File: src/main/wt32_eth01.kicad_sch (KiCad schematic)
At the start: 14 parts, among them J101 Conn_01x10, J105 Conn_01x06, U101 CD74HCT125M96, U202 WT32-ETH01-M3

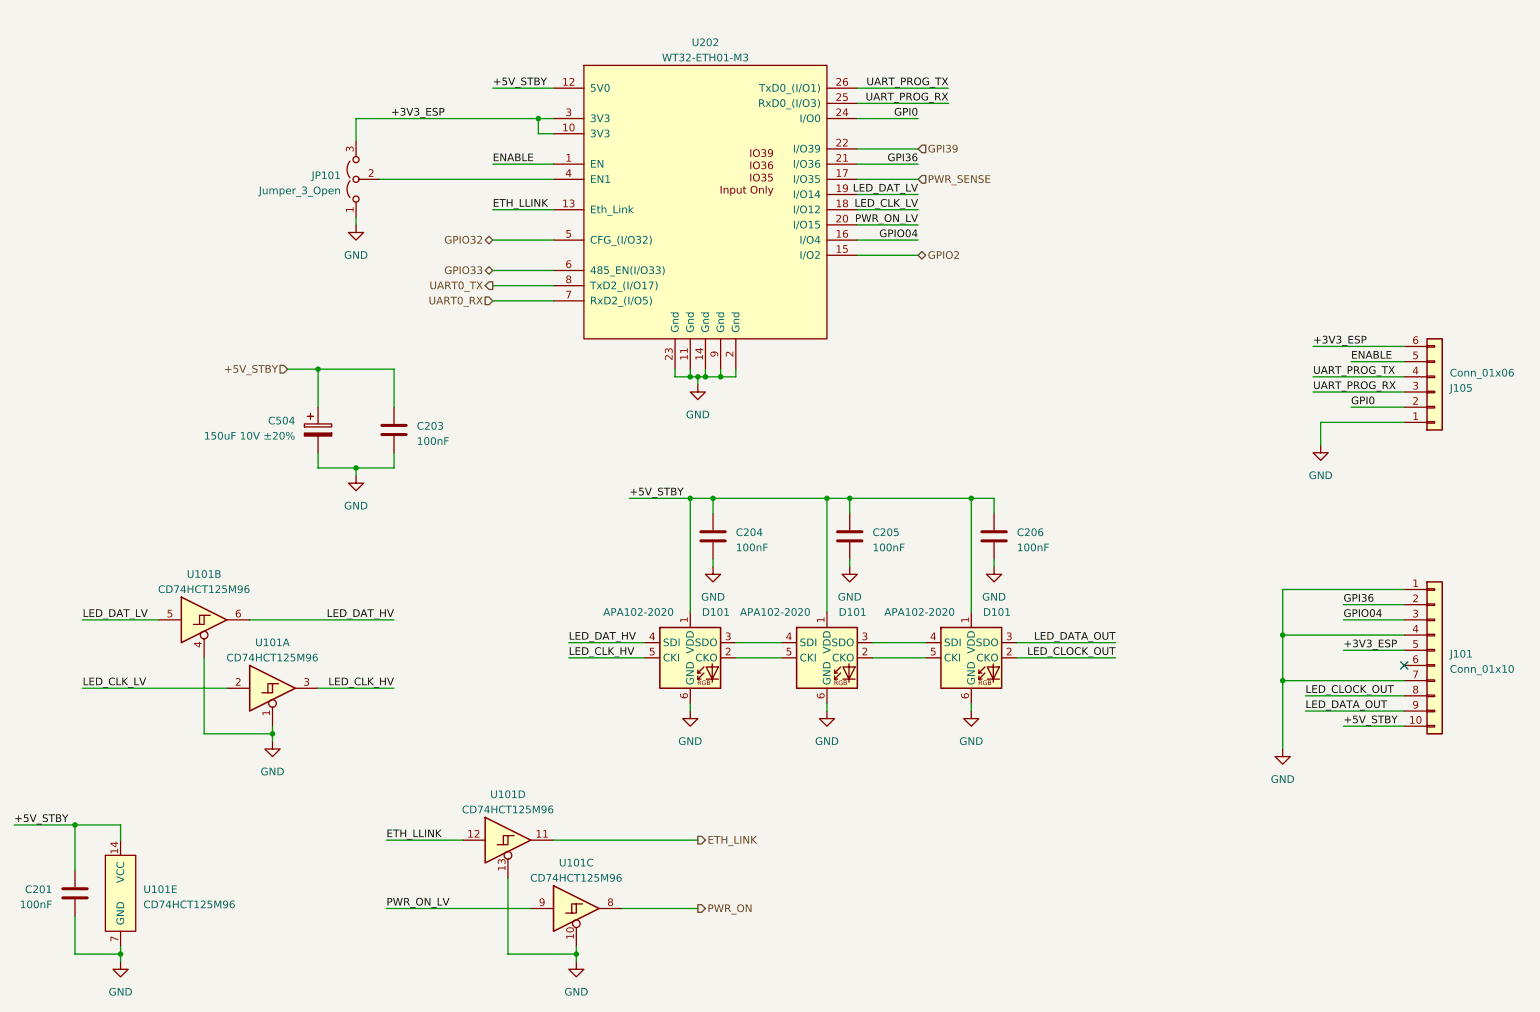
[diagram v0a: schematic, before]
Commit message: rev1.1.0
- J201 programming header
  - Add reset button
  - Add enable button
  - Make pinout compatible with USB-UART boards
    - Move GPI0 and ENABLE to testpoints
- Add power rail LED status indicators
  - 3V3_RUN
  - 3V3_ESP32
  - 5V_RUN
  - 5V_STBY
  - VBUS_[1-3]
- Remove JP201
- Add GPIO39 external pullup to 3V3
- Add pulldown to PWR_BUTTON (GPIO15)
- Add github link
- Add sillkscreen alignment fixes
- Add silkscreen default jumper marking
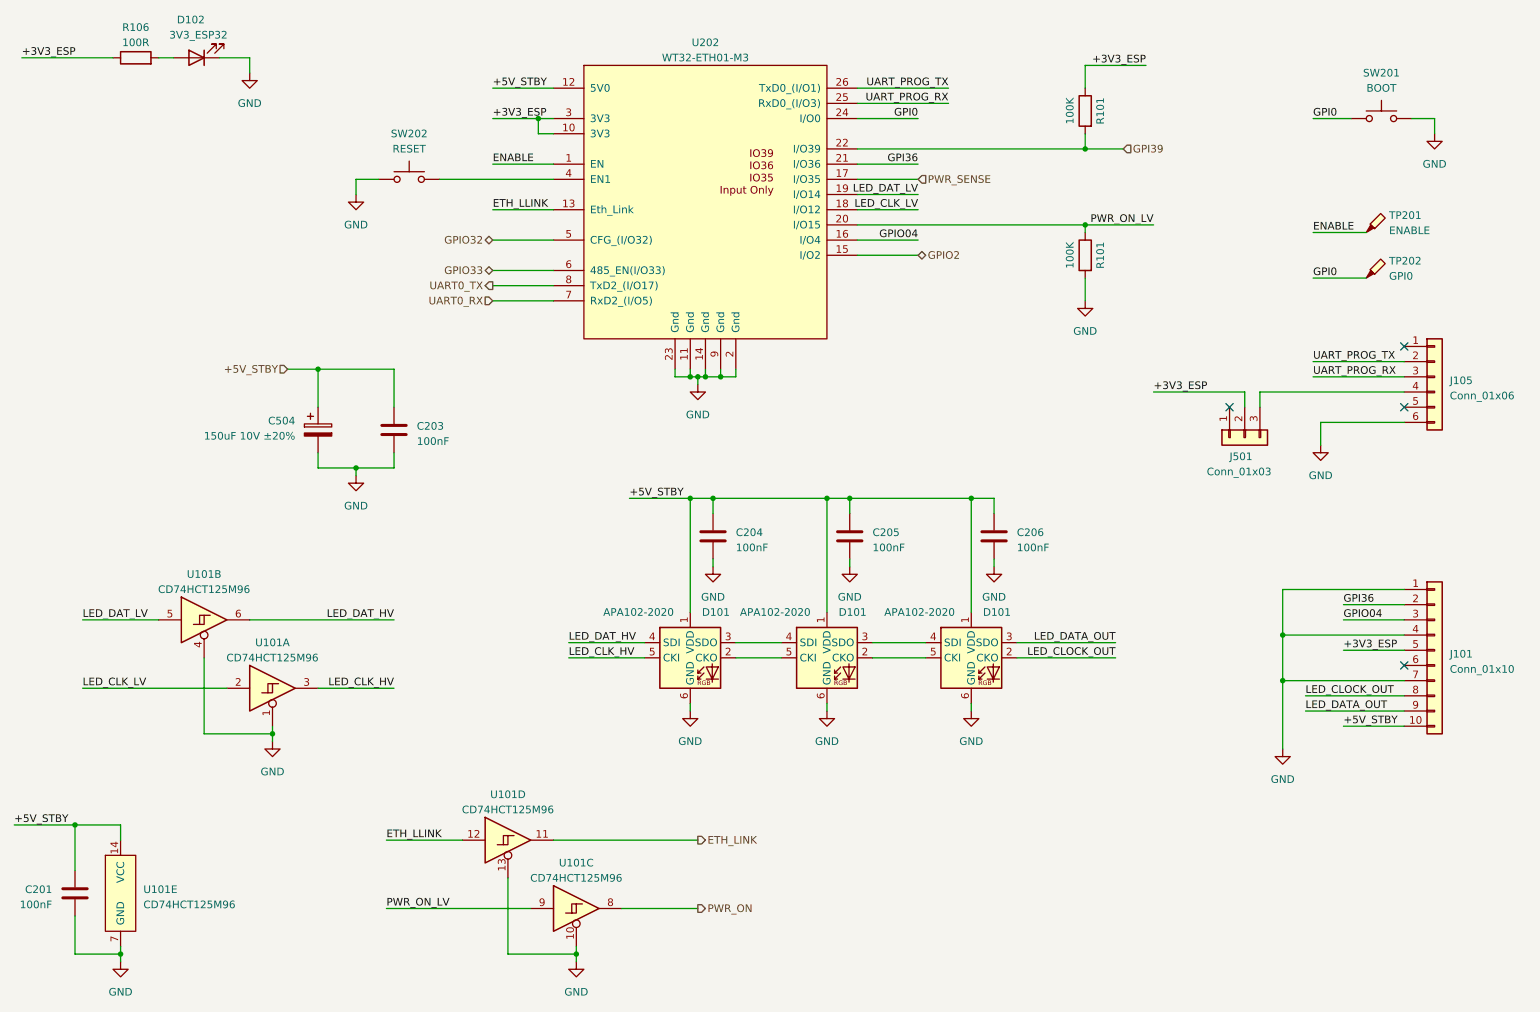
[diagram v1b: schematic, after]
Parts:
- removed JP101: Jumper_3_Open, Jumper:SolderJumper-3_P1.3mm_Open_RoundedPad1.0x1.5mm_NumberLabels, symbol Jumper:Jumper_3_Open
- added D102: 3V3_ESP32, LED_SMD:LED_0603_1608Metric, symbol Device:LED
- added J501: Conn_01x03, odroid_h3_uitx_adapter:PinHeader_1x03_P2.54mm_Vertical, symbol odroid_h3_uitx_adapter:Conn_01x03
- added R101 (x2): 100K, Resistor_SMD:R_0402_1005Metric, symbol Device:R
- added R106: 100R, Resistor_SMD:R_0402_1005Metric, symbol Device:R
- added SW201: BOOT, Button_Switch_THT:SW_PUSH_6mm_H5mm, symbol Switch:SW_Push
- added SW202: RESET, Button_Switch_THT:SW_PUSH_6mm_H5mm, symbol Switch:SW_Push
- added TP201: ENABLE, TestPoint:TestPoint_Pad_D2.0mm, symbol Connector:TestPoint_Probe
- added TP202: GPI0, TestPoint:TestPoint_Pad_D2.0mm, symbol Connector:TestPoint_Probe
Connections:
- net +3V3_ESP: now also J501.2 (Pin_2), R101.1, R106.1; no longer J105.6 (Pin_6)
- net ENABLE: now also TP201.1; no longer J105.5 (Pin_5)
- net GND: now also J105.6 (Pin_6), D102.1 (K), R101.2, SW201.2, SW202.2; no longer J105.1 (Pin_1)
- net GPI0: now also SW201.1, TP202.1; no longer J105.2 (Pin_2)
- net GPI39: now also R101.2
- net PWR_ON_LV: now also R101.1
- net UART_PROG_TX: now also J105.2 (Pin_2); no longer J105.4 (Pin_4)
- net at U202.4 (EN1): now also SW202.1
- new net: J105.4 (Pin_4), J501.3 (Pin_3)
- new net: D102.2 (A), R106.2
- no-connect marks 1 -> 4

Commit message: Additions and fixes:
Add:
- Add power rail LED status indicators
- Buffered LED on ETH_LINK
- GPIO14 and GPIO12 on header
- GPIO14 5V buffered output on header
- Testpoints for GPIO0 and ESP32_ENABLE pin
- Reset and Boot switches
- ESP PWR selector switch
- USB Type-C PD input (5V) for ESP32
- 1.1A Fuse for USB PD input
- Add spot for BIOS battery on silk
- Add silkscreen default jumper marking
- Add GPIO39 external pullup to 3V3
- Add pulldown to PWR_BUTTON (GPIO15)
- Add silkscreen github link

Fixes:
- Clarify things on silk
- Make pinout compatible with USB-UART boards
  - Move GPI0 and ENABLE to testpoints
- Silkscreen alignment fixes

Removed:
- 3 APA102 LEDs
- Remove JP201
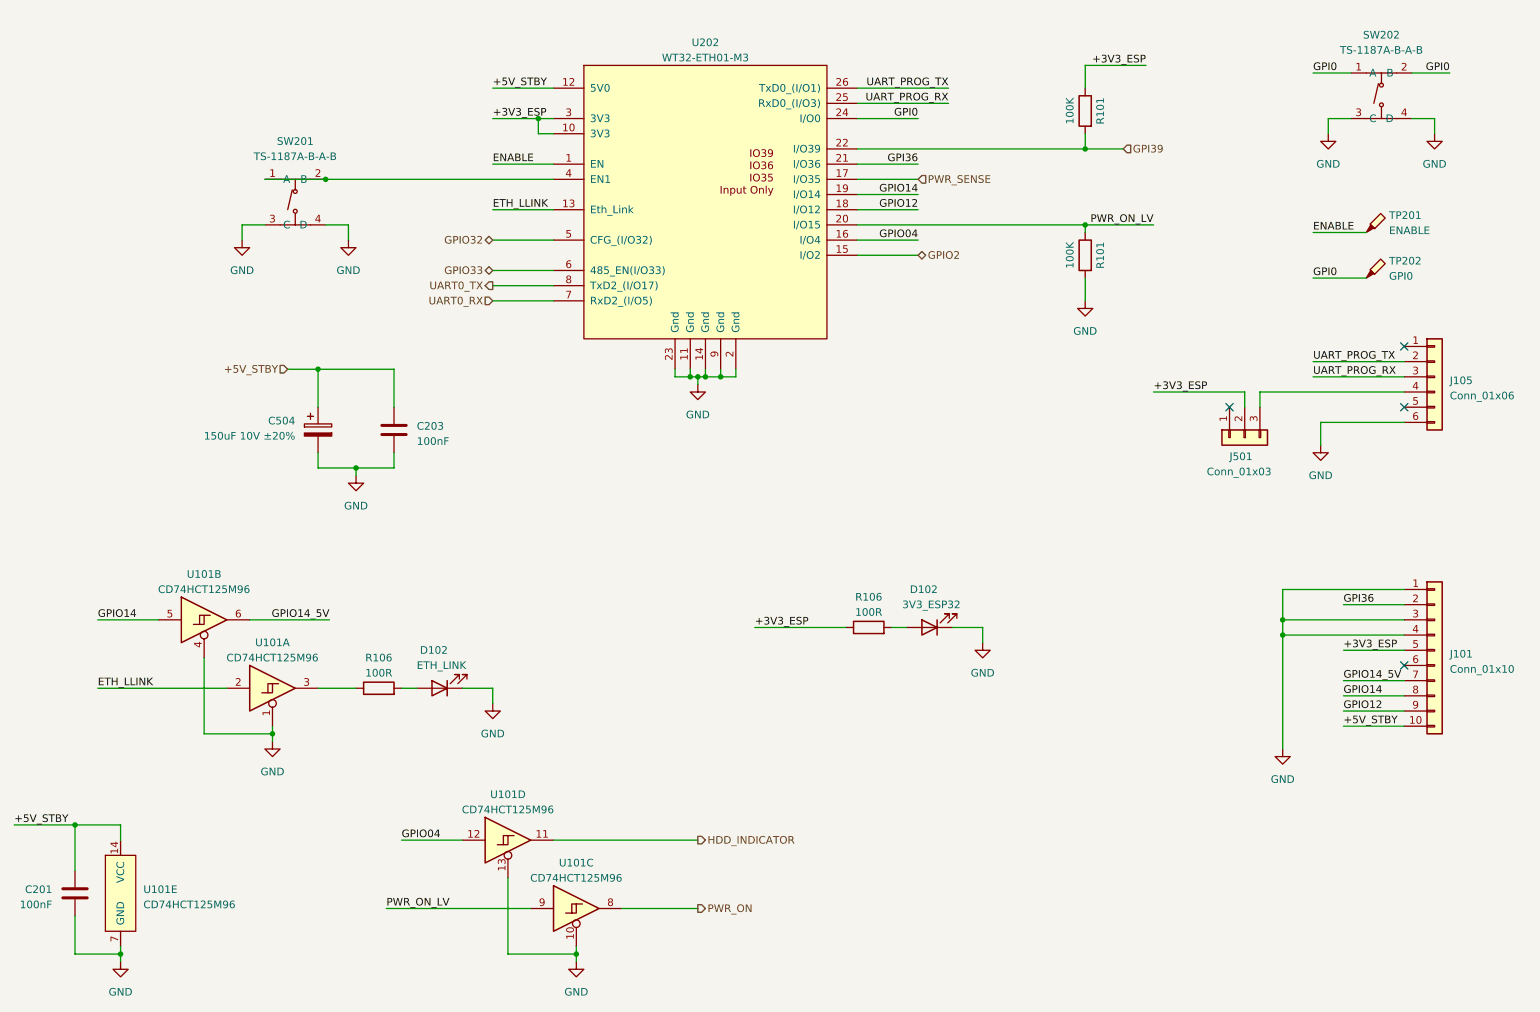
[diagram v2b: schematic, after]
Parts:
- removed C204, C205, C206: 100nF, Capacitor_SMD:C_0402_1005Metric, symbol Device:C
- removed D101 (x3): APA102-2020, odroid_h3_uitx_adapter:LED-APA102-2020, symbol odroid_h3_uitx_adapter:APA102-2020
- removed SW201: BOOT, Button_Switch_THT:SW_PUSH_6mm_H5mm, symbol Switch:SW_Push
- removed SW202: RESET, Button_Switch_THT:SW_PUSH_6mm_H5mm, symbol Switch:SW_Push
- added D102: ETH_LINK, LED_SMD:LED_0603_1608Metric, symbol Device:LED
- added R106: 100R, Resistor_SMD:R_0402_1005Metric, symbol Device:R
- added SW201, SW202: TS-1187A-B-A-B, easyeda2kicad:SW-SMD_4P-L5.1-W5.1-P3.70-LS6.5-TL-2, symbol easyeda2kicad:TS-1187A-B-A-B
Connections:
- net LED_DATA_OUT is gone; now on net GPIO12: J101.9 (Pin_9)
- net LED_DAT_LV is gone; now on net GPIO14: U101.5, U202.19 (I/O14)
- net ETH_LLINK: now also U101.2; no longer U101.12
- net GND: now also J101.3 (Pin_3), D102.1 (K), SW201.3 (C), SW201.4 (D), SW202.3 (C), SW202.4 (D); no longer J101.7 (Pin_7)
- net GPI0: now also SW202.1 (A), SW202.2 (B)
- net GPIO04: now also U101.12; no longer J101.3 (Pin_3)
- net at U202.4 (EN1): now also SW201.1 (A), SW201.2 (B)
- net ETH_LINK renamed HDD_INDICATOR
- net LED_CLK_HV: no longer names the net of U101.3
- net LED_CLK_HV: now also R106.1
- net LED_CLK_LV renamed GPIO12
- net GPIO12: no longer U101.2
- net LED_CLOCK_OUT renamed GPIO14
- net LED_DAT_HV renamed GPIO14_5V
- net GPIO14_5V: now also J101.7 (Pin_7)
- new net: D102.2 (A), R106.2
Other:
- moved on the sheet: D102, R106
